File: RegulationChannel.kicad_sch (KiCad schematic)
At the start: 1 part

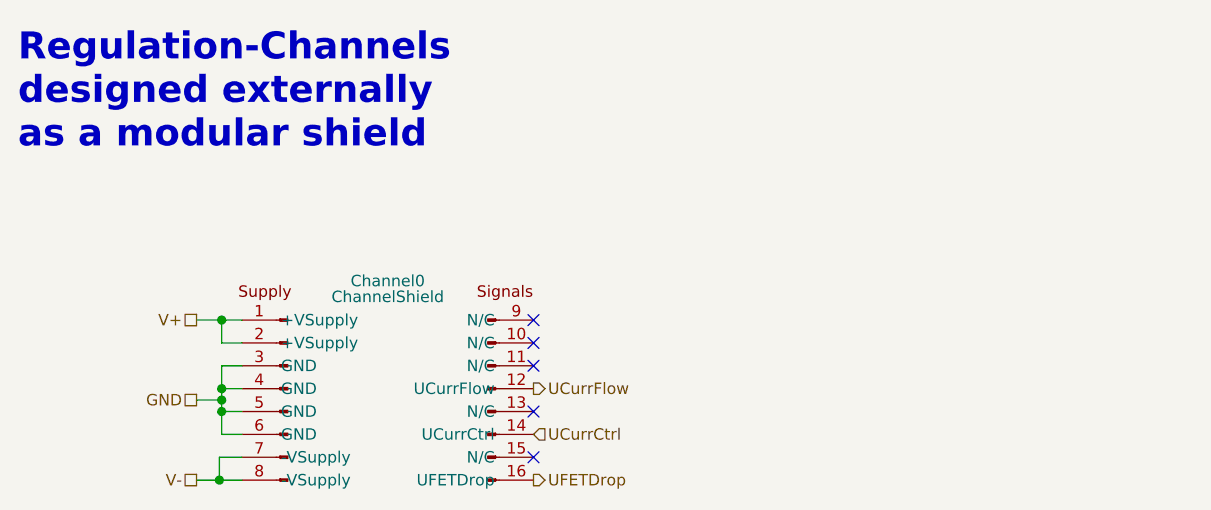
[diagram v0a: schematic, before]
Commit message: FEAR-16 V2.2
PCB-Changes:
 - Added rudimentary "load-balancer" (not really a balancer, but should avoid the DC/DC from regulating against each other!)
 - Added optional GND-jumpers to the N/C pins of the shields
 - Modified amplification adjustment:
   -> Added a offset resistor in row to the trim-poti for amplification for finer amp-tuning
   -> Reduced trim-poti-value from 1Meg -> 50k (20x finer adjustment-range)
      Poti can in the range of:
      - 30k (min) for being able to reach the correct amplification
      - 50k (max) for having at least 20x finer tune-range and a bit of reserve, as 30k is pretty thight on tolerance

Misc.:
 - Added LICENSE.md
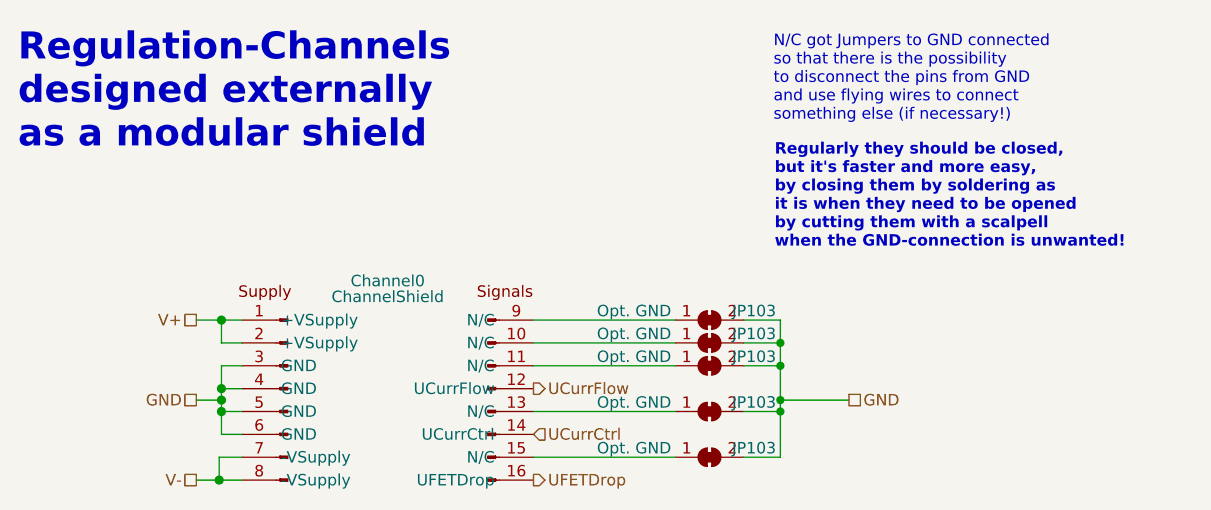
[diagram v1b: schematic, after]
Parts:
- added JP103 (x5): Opt. GND, Jumper:SolderJumper-2_P1.3mm_Open_RoundedPad1.0x1.5mm, symbol Jumper:SolderJumper_2_Bridged
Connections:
- net GND: now also JP103.2 (B), JP103.2 (B), JP103.2 (B), JP103.2 (B), JP103.2 (B)
- net at Channel0.10 (N/C): now also JP103.1 (A)
- net at Channel0.11 (N/C): now also JP103.1 (A)
- net at Channel0.13 (N/C): now also JP103.1 (A)
- net at Channel0.15 (N/C): now also JP103.1 (A)
- net at Channel0.9 (N/C): now also JP103.1 (A)
- no-connect marks 5 -> 0
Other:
- note added: "N/C got Jumpers to GND connected so that there is the possibility to disconnect the pins from GND and use flying wires to connect something else (if necessary!)"
- note added: "Regularly they should be closed, but it's faster and more easy, by closing them by soldering as it is when they need to be opened by cutting them with a scalpell when the GND-connection is unwanted!"

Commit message: Fixed ADP2370 designator
ADP2370 has a bunch of fixed output voltages and an adjustable model.
We use the adjustable model, so we fixed the name matching with the correct model-name.
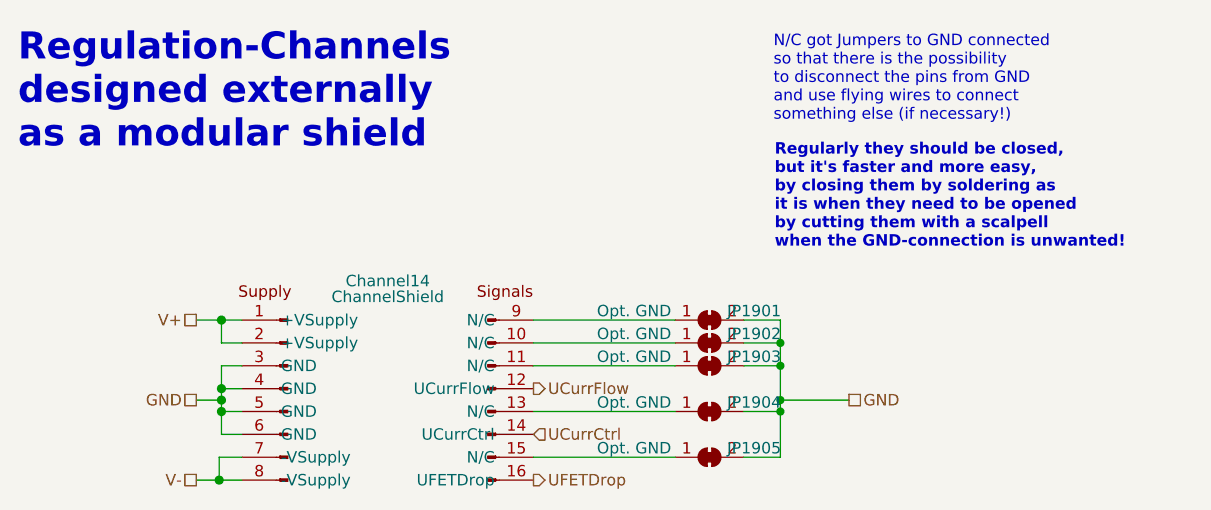
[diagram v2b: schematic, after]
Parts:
- renumbered Channel0 to Channel14, JP103 to JP1901, JP103 to JP1902, JP103 to JP1903, JP103 to JP1904, JP103 to JP1905
